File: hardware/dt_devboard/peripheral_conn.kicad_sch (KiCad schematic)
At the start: 2 parts

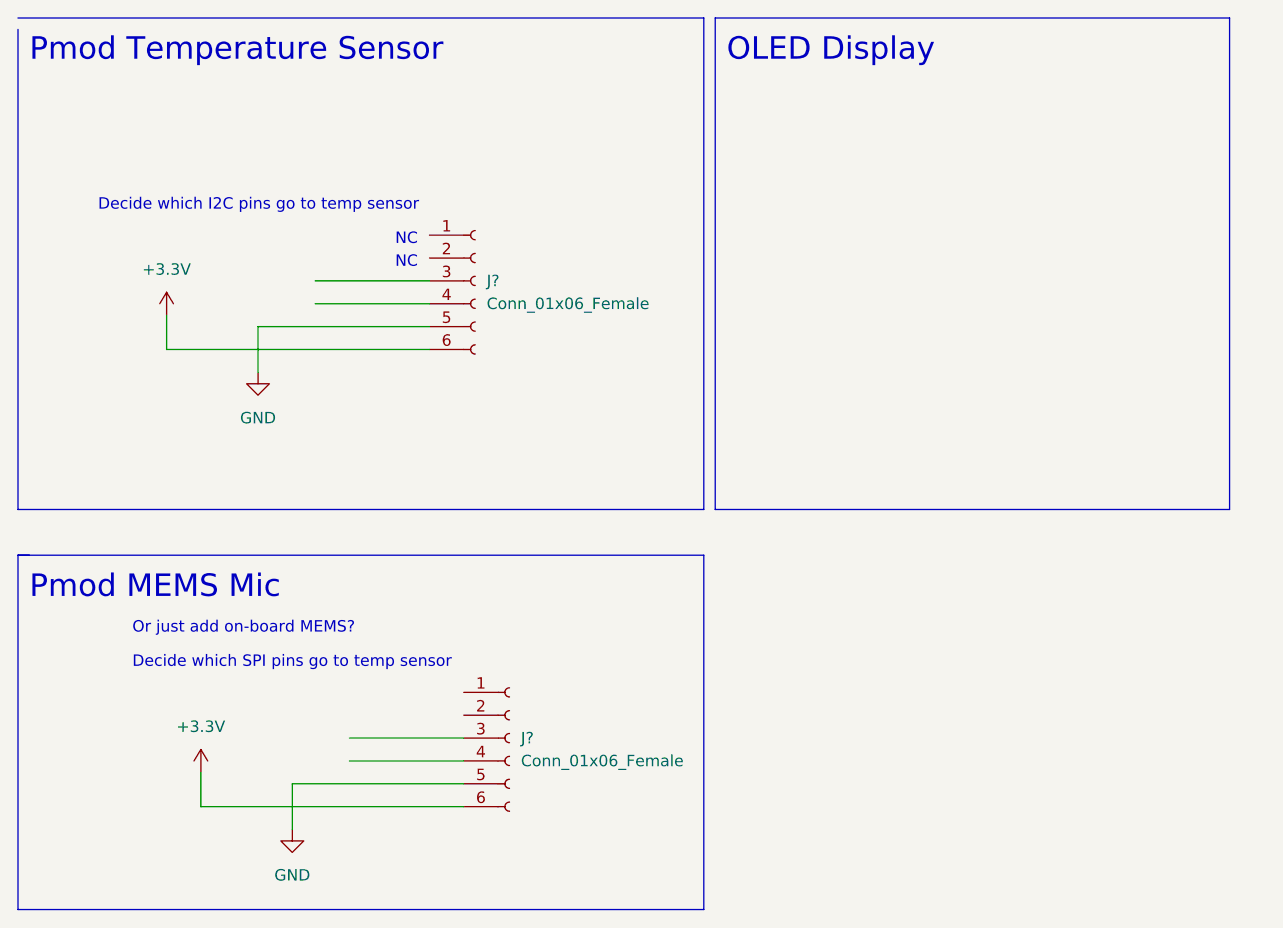
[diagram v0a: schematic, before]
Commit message: added camera module connector
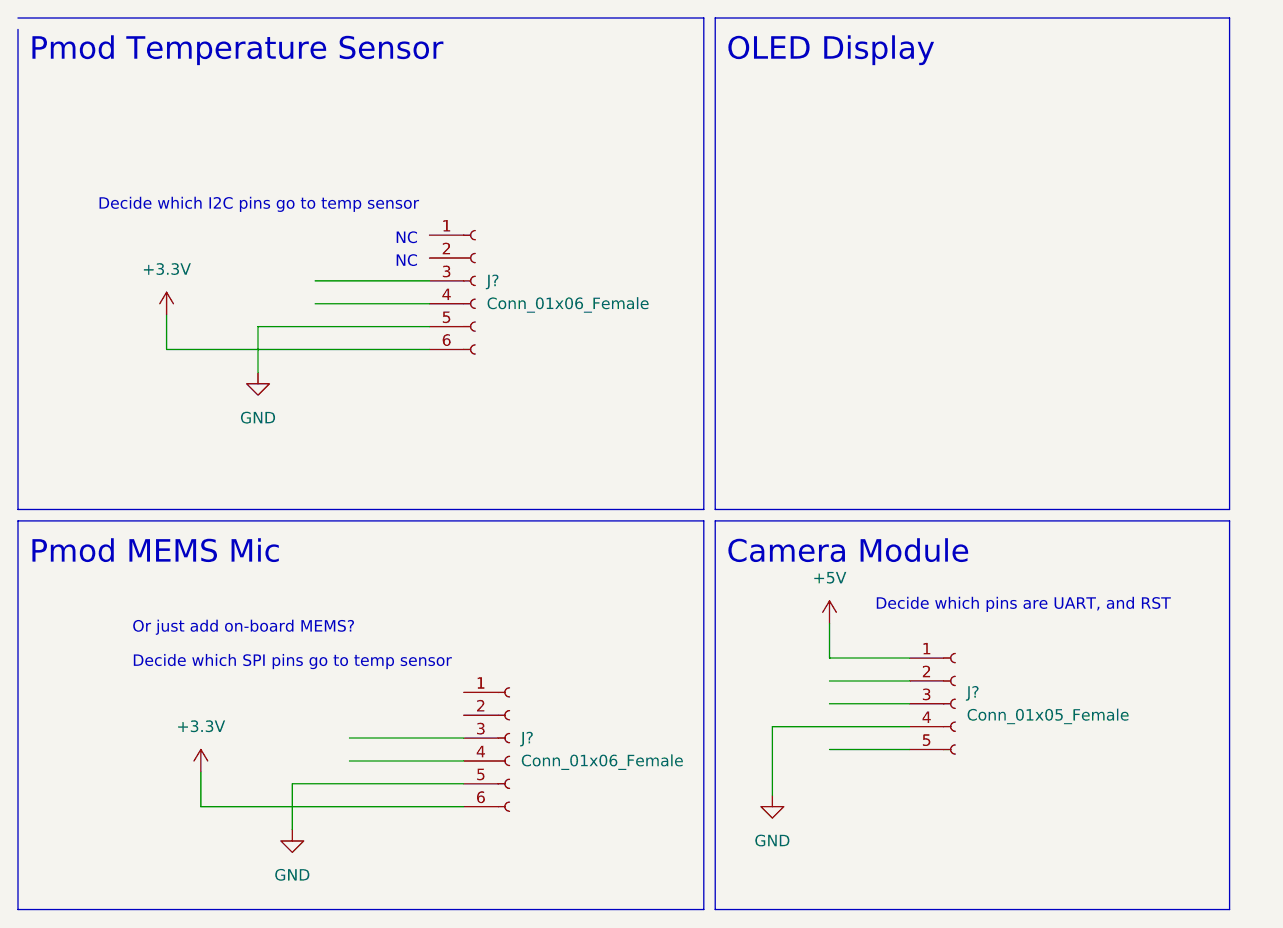
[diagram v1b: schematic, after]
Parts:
- added J?: Conn_01x05_Female, symbol Connector:Conn_01x05_Female
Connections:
- net GND: now also J?.4 (Pin_4)
- new net +5V: J?.1 (Pin_1)
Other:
- note added: "Camera Module"
- note added: "Decide which pins are UART, and RST"
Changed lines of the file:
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@@
     (stroke (width 0) (type default) (color 0 0 0 0))
   )
-  (polyline (pts (xy 97.79 81.28) (xy 97.79 120.65))
+  (wire (pts (xy 105.41 100.33) (xy 105.41 107.95))
+    (stroke (width 0) (type default) (color 0 0 0 0))
+  )
+  (polyline (pts (xy 97.79 77.47) (xy 97.79 120.65))
     (stroke (width 0) (type default) (color 0 0 0 0))
   )
@@
     (stroke (width 0) (type default) (color 0 0 0 0))
   )
+  (wire (pts (xy 111.76 88.9) (xy 111.76 92.71))
+    (stroke (width 0) (type default) (color 0 0 0 0))
+  )
   (wire (pts (xy 38.1 58.42) (xy 67.31 58.42))
     (stroke (width 0) (type default) (color 0 0 0 0))
   )
-  (polyline (pts (xy 21.59 81.28) (xy 22.86 81.28))
+  (polyline (pts (xy 99.06 120.65) (xy 156.21 120.65))
     (stroke (width 0) (type default) (color 0 0 0 0))
   )
@@
     (stroke (width 0) (type default) (color 0 0 0 0))
   )
+  (wire (pts (xy 111.76 95.25) (xy 120.65 95.25))
+    (stroke (width 0) (type default) (color 0 0 0 0))
+  )
   (polyline (pts (xy 21.59 21.59) (xy 97.79 21.59))
     (stroke (width 0) (type default) (color 0 0 0 0))
   )
+  (polyline (pts (xy 99.06 77.47) (xy 156.21 77.47))
+    (stroke (width 0) (type default) (color 0 0 0 0))
+  )
   (polyline (pts (xy 99.06 76.2) (xy 99.06 21.59))
     (stroke (width 0) (type default) (color 0 0 0 0))
   )
+  (polyline (pts (xy 156.21 77.47) (xy 156.21 120.65))
+    (stroke (width 0) (type default) (color 0 0 0 0))
+  )
+  (wire (pts (xy 120.65 100.33) (xy 105.41 100.33))
+    (stroke (width 0) (type default) (color 0 0 0 0))
+  )
+  (wire (pts (xy 111.76 92.71) (xy 120.65 92.71))
+    (stroke (width 0) (type default) (color 0 0 0 0))
+  )
   (wire (pts (xy 41.91 109.22) (xy 71.12 109.22))
     (stroke (width 0) (type default) (color 0 0 0 0))
@@
     (stroke (width 0) (type default) (color 0 0 0 0))
   )
+  (wire (pts (xy 111.76 97.79) (xy 120.65 97.79))
+    (stroke (width 0) (type default) (color 0 0 0 0))
+  )
   (wire (pts (xy 48.26 55.88) (xy 67.31 55.88))
     (stroke (width 0) (type default) (color 0 0 0 0))
@@
     (stroke (width 0) (type default) (color 0 0 0 0))
   )
-  (polyline (pts (xy 21.59 81.28) (xy 97.79 81.28))
+  (wire (pts (xy 111.76 102.87) (xy 120.65 102.87))
+    (stroke (width 0) (type default) (color 0 0 0 0))
+  )
+  (polyline (pts (xy 21.59 77.47) (xy 97.79 77.47))
     (stroke (width 0) (type default) (color 0 0 0 0))
   )
@@
     (stroke (width 0) (type default) (color 0 0 0 0))
   )
-  (polyline (pts (xy 21.59 120.65) (xy 21.59 81.28))
+  (polyline (pts (xy 21.59 120.65) (xy 21.59 77.47))
     (stroke (width 0) (type default) (color 0 0 0 0))
   )
@@
     (stroke (width 0) (type default) (color 0 0 0 0))
   )
+  (polyline (pts (xy 99.06 120.65) (xy 99.06 77.47))
+    (stroke (width 0) (type default) (color 0 0 0 0))
+  )
   (text "Decide which I2C pins go to temp sensor\n" (at 30.48 43.18 0)
     (effects (font (size 1.27 1.27)) (justify left bottom))
@@
     (effects (font (size 1.27 1.27)) (justify left bottom))
   )
-  (text "Pmod MEMS Mic\n" (at 22.86 86.36 0)
+  (text "Pmod MEMS Mic\n" (at 22.86 82.55 0)
     (effects (font (size 2.5 2.5)) (justify left bottom))
   )
@@
     (effects (font (size 1.27 1.27)) (justify left bottom))
   )
+  (text "Camera Module\n" (at 100.33 82.55 0)
+    (effects (font (size 2.5 2.5)) (justify left bottom))
+  )
   (text "Pmod Temperature Sensor" (at 22.86 26.67 0)
     (effects (font (size 2.5 2.5)) (justify left bottom))
@@
   (text "OLED Display\n" (at 100.33 26.67 0)
     (effects (font (size 2.5 2.5)) (justify left bottom))
+  )
+  (text "Decide which pins are UART, and RST\n" (at 116.84 87.63 0)
+    (effects (font (size 1.27 1.27)) (justify left bottom))
   )
   (symbol (lib_id "Connector:Conn_01x06_Female") (at 76.2 101.6 0) (unit 1)
@@
     (pin "6")
   )
+  (symbol (lib_id "power:+5V") (at 111.76 88.9 0) (unit 1)
+    (in_bom yes) (on_board yes) (fields_autoplaced)
+    (property "Reference" "#PWR?" (id 0) (at 111.76 92.71 0)
+      (effects (font (size 1.27 1.27)) hide)
+    )
+    (property "Value" "+5V" (id 1) (at 111.76 83.82 0))
+    (property "Footprint" "" (id 2) (at 111.76 88.9 0)
+      (effects (font (size 1.27 1.27)) hide)
+    )
+    (property "Datasheet" "" (id 3) (at 111.76 88.9 0)
+      (effects (font (size 1.27 1.27)) hide)
+    )
+    (pin "1")
+  )
+  (symbol (lib_id "Connector:Conn_01x05_Female") (at 125.73 97.79 0) (unit 1)
+    (in_bom yes) (on_board yes) (fields_autoplaced)
+    (property "Reference" "J?" (id 0) (at 127 96.5199 0)
+      (effects (font (size 1.27 1.27)) (justify left))
+    )
+    (property "Value" "Conn_01x05_Female" (id 1) (at 127 99.0599 0)
+      (effects (font (size 1.27 1.27)) (justify left))
+    )
+    (property "Footprint" "" (id 2) (at 125.73 97.79 0)
+      (effects (font (size 1.27 1.27)) hide)
+    )
+    (property "Datasheet" "~" (id 3) (at 125.73 97.79 0)
+      (effects (font (size 1.27 1.27)) hide)
+    )
+    (pin "1")
+    (pin "2")
+    (pin "3")
+    (pin "4")
+    (pin "5")
+  )
   (symbol (lib_id "power:GND") (at 52.07 111.76 0) (unit 1)
     (in_bom yes) (on_board yes) (fields_autoplaced)
@@
       (effects (font (size 1.27 1.27)) hide)
     )
+    (pin "1")
+  )
+  (symbol (lib_id "power:GND") (at 105.41 107.95 0) (unit 1)
+    (in_bom yes) (on_board yes) (fields_autoplaced)
+    (property "Reference" "#PWR?" (id 0) (at 105.41 114.3 0)
+      (effects (font (size 1.27 1.27)) hide)
+    )
+    (property "Value" "GND" (id 1) (at 105.41 113.03 0))
+    (property "Footprint" "" (id 2) (at 105.41 107.95 0)
+      (effects (font (size 1.27 1.27)) hide)
+    )
+    (property "Datasheet" "" (id 3) (at 105.41 107.95 0)
+      (effects (font (size 1.27 1.27)) hide)
+    )

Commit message: added I2C, SPI and UART signals
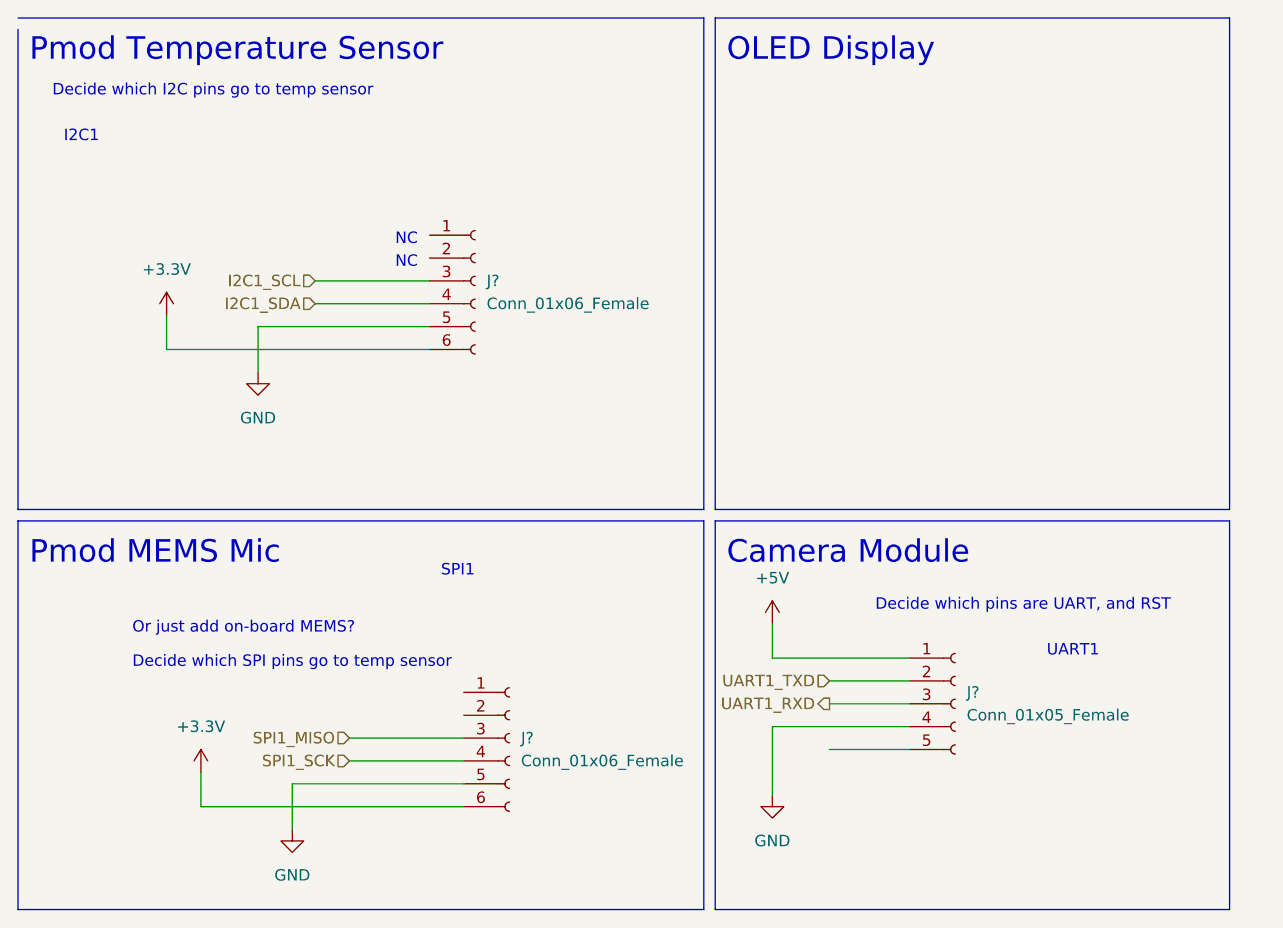
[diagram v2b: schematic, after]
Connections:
- net SPI1_MISO: now reaches J?.3 (Pin_3)
- net SPI1_SCK: now reaches J?.4 (Pin_4)
- net UART1_TXD: now reaches J?.2 (Pin_2)
- net UART1_RXD: now reaches J?.3 (Pin_3)
- net I2C1_SCL: now reaches J?.3 (Pin_3)
- net I2C1_SDA: now reaches J?.4 (Pin_4)
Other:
- note added: "I2C1"
- note added: "SPI1"
- note added: "UART1"
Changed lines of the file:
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@@
     (stroke (width 0) (type default) (color 0 0 0 0))
   )
-  (wire (pts (xy 111.76 88.9) (xy 111.76 92.71))
+  (wire (pts (xy 105.41 88.9) (xy 105.41 92.71))
     (stroke (width 0) (type default) (color 0 0 0 0))
   )
@@
     (stroke (width 0) (type default) (color 0 0 0 0))
   )
-  (wire (pts (xy 111.76 92.71) (xy 120.65 92.71))
+  (wire (pts (xy 105.41 92.71) (xy 120.65 92.71))
     (stroke (width 0) (type default) (color 0 0 0 0))
   )
@@
     (stroke (width 0) (type default) (color 0 0 0 0))
   )
-  (text "Decide which I2C pins go to temp sensor\n" (at 30.48 43.18 0)
+  (text "Decide which I2C pins go to temp sensor\n" (at 25.4 30.48 0)
     (effects (font (size 1.27 1.27)) (justify left bottom))
   )
@@
     (effects (font (size 1.27 1.27)) (justify left bottom))
   )
+  (text "SPI1" (at 68.58 83.82 0)
+    (effects (font (size 1.27 1.27)) (justify left bottom))
+  )
+  (text "UART1" (at 135.89 92.71 0)
+    (effects (font (size 1.27 1.27)) (justify left bottom))
+  )
   (text "Camera Module\n" (at 100.33 82.55 0)
     (effects (font (size 2.5 2.5)) (justify left bottom))
@@
   (text "Decide which pins are UART, and RST\n" (at 116.84 87.63 0)
     (effects (font (size 1.27 1.27)) (justify left bottom))
+  )
+  (text "I2C1" (at 26.67 35.56 0)
+    (effects (font (size 1.27 1.27)) (justify left bottom))
+  )
+  (hierarchical_label "I2C1_SCL" (shape input) (at 54.61 50.8 180)
+    (effects (font (size 1.27 1.27)) (justify right))
+  )
+  (hierarchical_label "SPI1_MISO" (shape input) (at 58.42 101.6 180)
+    (effects (font (size 1.27 1.27)) (justify right))
+  )
+  (hierarchical_label "I2C1_SDA" (shape input) (at 54.61 53.34 180)
+    (effects (font (size 1.27 1.27)) (justify right))
+  )
+  (hierarchical_label "UART1_RXD" (shape output) (at 111.76 97.79 180)
+    (effects (font (size 1.27 1.27)) (justify right))
+  )
+  (hierarchical_label "SPI1_SCK" (shape input) (at 58.42 104.14 180)
+    (effects (font (size 1.27 1.27)) (justify right))
+  )
+  (hierarchical_label "UART1_TXD" (shape input) (at 111.76 95.25 180)
+    (effects (font (size 1.27 1.27)) (justify right))
   )
   (symbol (lib_id "Connector:Conn_01x06_Female") (at 76.2 101.6 0) (unit 1)
@@
     (pin "6")
   )
-  (symbol (lib_id "power:+5V") (at 111.76 88.9 0) (unit 1)
-    (in_bom yes) (on_board yes) (fields_autoplaced)
-    (property "Reference" "#PWR?" (id 0) (at 111.76 92.71 0)
-      (effects (font (size 1.27 1.27)) hide)
-    )
-    (property "Value" "+5V" (id 1) (at 111.76 83.82 0))
-    (property "Footprint" "" (id 2) (at 111.76 88.9 0)
-      (effects (font (size 1.27 1.27)) hide)
-    )
-    (property "Datasheet" "" (id 3) (at 111.76 88.9 0)
+  (symbol (lib_id "power:+5V") (at 105.41 88.9 0) (unit 1)
+    (in_bom yes) (on_board yes) (fields_autoplaced)
+    (property "Reference" "#PWR?" (id 0) (at 105.41 92.71 0)
+      (effects (font (size 1.27 1.27)) hide)
+    )
+    (property "Value" "+5V" (id 1) (at 105.41 83.82 0))
+    (property "Footprint" "" (id 2) (at 105.41 88.9 0)
+      (effects (font (size 1.27 1.27)) hide)
+    )
+    (property "Datasheet" "" (id 3) (at 105.41 88.9 0)
       (effects (font (size 1.27 1.27)) hide)
     )
@@
     (pin "1")
   )
+  (sheet_instances
+    (path "/" (page "1"))
+  )
+  (symbol_instances
+    (path "/2bc3dab7-b392-4f4b-986a-4e04dd17dd81"
+      (reference "#PWR?") (unit 1) (value "+5V") (footprint "")
+    )
+    (path "/5c3fbc86-b745-4733-8ef5-b40aa9974c3c"
+      (reference "#PWR?") (unit 1) (value "GND") (footprint "")
+    )
+    (path "/607e16ab-128e-4b86-a730-5342459a2b2b"
+      (reference "#PWR?") (unit 1) (value "+3.3V") (footprint "")
+    )
+    (path "/7f32e42a-2623-416f-acda-f0efd901b01f"
+      (reference "#PWR?") (unit 1) (value "GND") (footprint "")
+    )
+    (path "/b78957c1-d667-4d5c-85d2-989d524d1809"
+      (reference "#PWR?") (unit 1) (value "GND") (footprint "")
+    )
+    (path "/ef3abe03-d68b-4855-bc8f-417487ded968"
+      (reference "#PWR?") (unit 1) (value "+3.3V") (footprint "")
+    )
+    (path "/15613572-e2c0-4cb3-97c2-7f932dbd6ac4"
+      (reference "J?") (unit 1) (value "Conn_01x06_Female") (footprint "")
+    )
+    (path "/57ac986f-5fd8-4d62-b48b-c429dac1b50a"
+      (reference "J?") (unit 1) (value "Conn_01x05_Female") (footprint "")
+    )
+    (path "/c1cbdd6e-51f3-4b37-beed-34ae3ed00775"
+      (reference "J?") (unit 1) (value "Conn_01x06_Female") (footprint "")
+    )
+  )
 )
